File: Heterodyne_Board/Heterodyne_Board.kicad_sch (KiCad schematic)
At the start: 56 parts, among them J1 AVR-ISP-6, J2 Speaker, J3 SWITCH, J4 LED, J6 AudioJack2_Ground_Switch, J7 Barrel_Jack, SW1 SW_SPST, SW2 SW_SPST, U1 ATtiny85-20P, U2 TLV9054xD, U3 AP2112K-3.3, U4 LM386, U5 W25X40CLSN

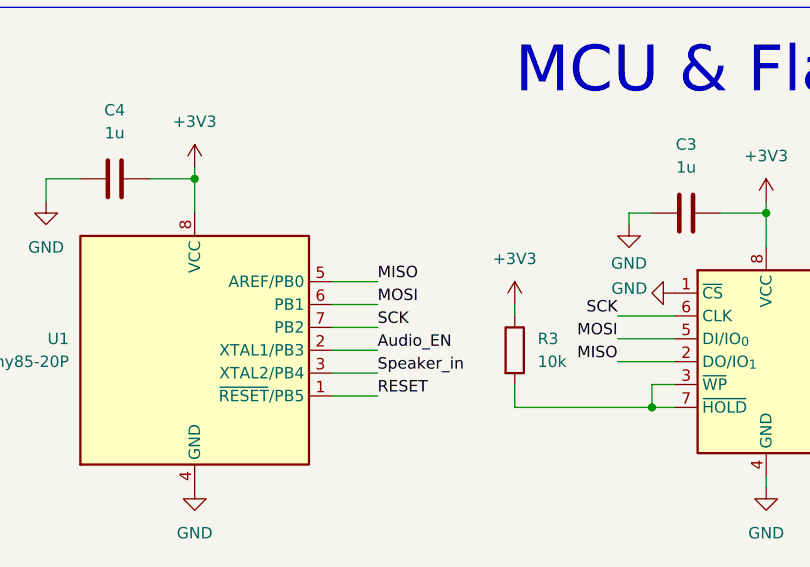
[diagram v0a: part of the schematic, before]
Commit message: Fixed MOSI/MISO line, lab entry for 3-1
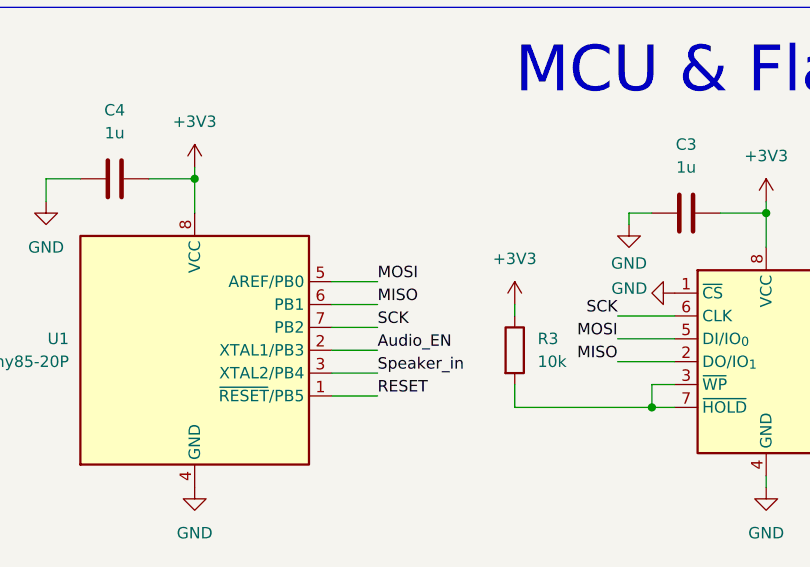
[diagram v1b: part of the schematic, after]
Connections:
- net MISO: now also U1.6 (PB1); no longer U1.5 (AREF/PB0)
- net MOSI: now also U1.5 (AREF/PB0); no longer U1.6 (PB1)
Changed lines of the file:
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@@
 		)
 	)
-	(label "MISO"
+	(label "MOSI"
 		(at 129.54 43.18 0)
 		(effects
@@
 		)
 	)
-	(label "MOSI"
+	(label "MISO"
 		(at 129.54 45.72 0)
 		(effects

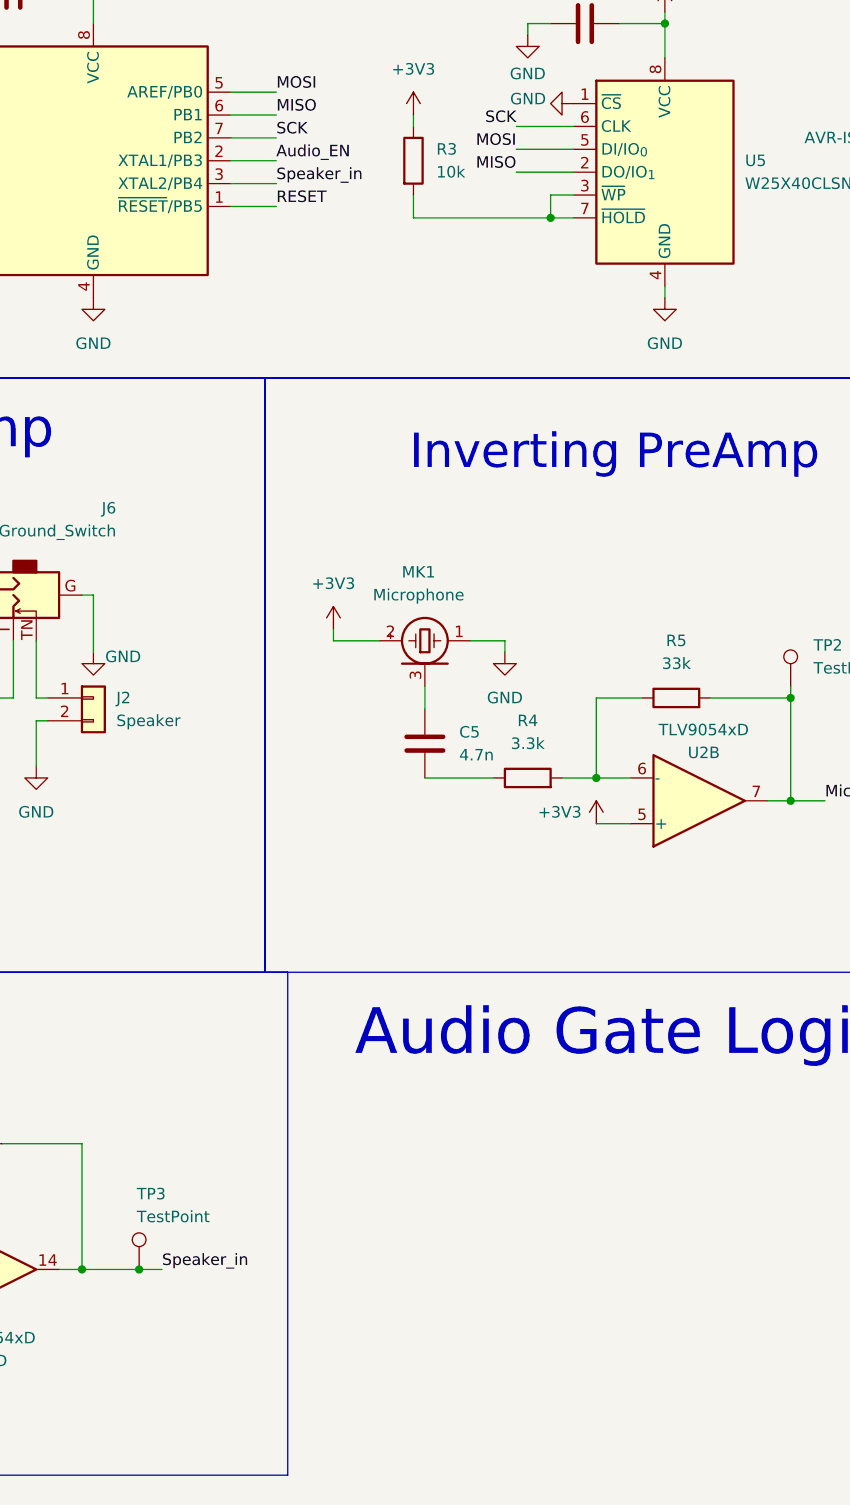
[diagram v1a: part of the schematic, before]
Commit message: added switch between mcu and mixer for audio output definition
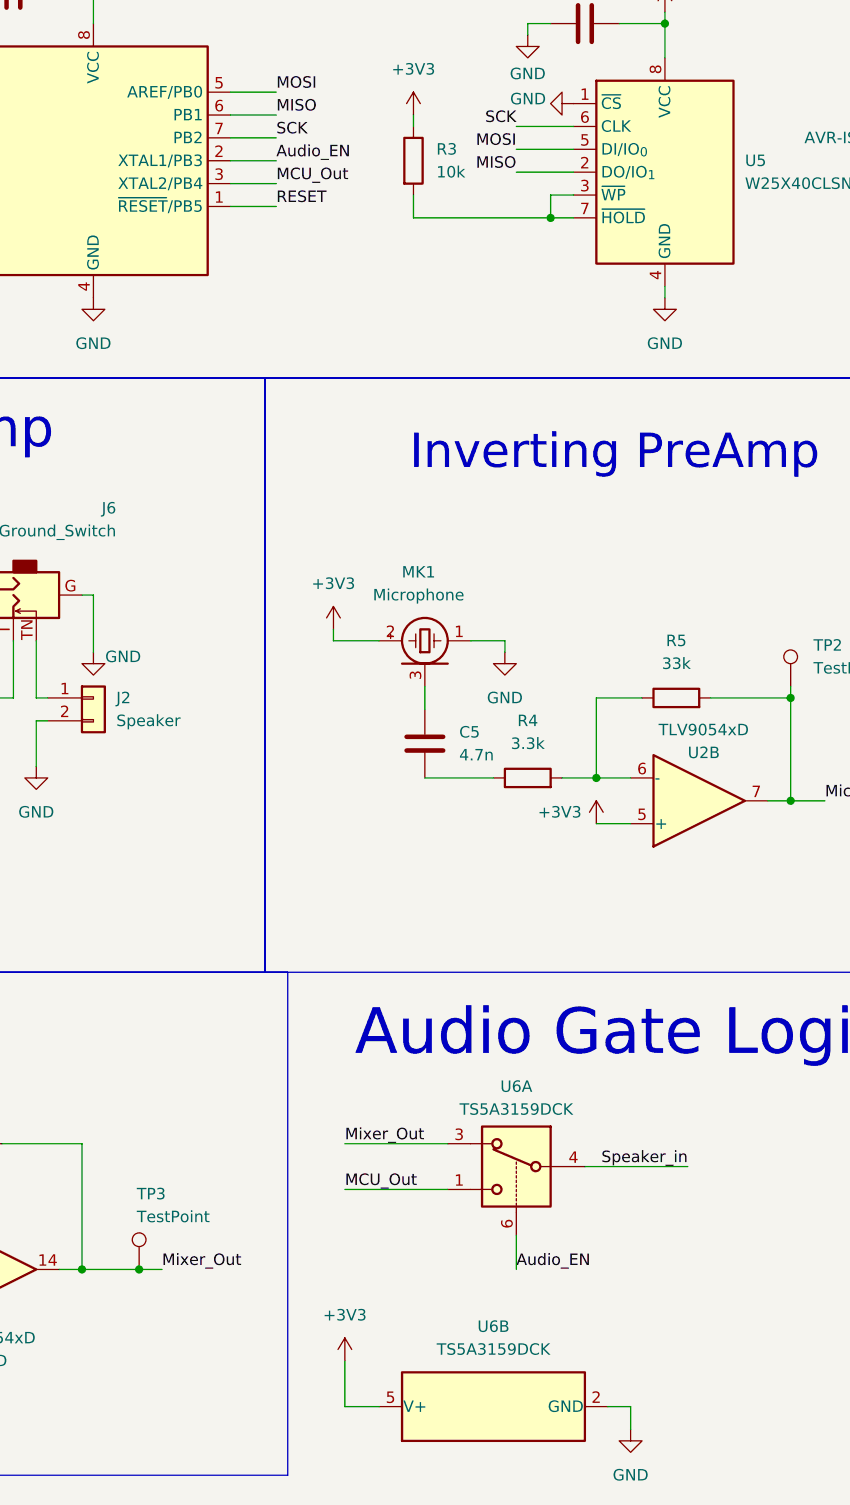
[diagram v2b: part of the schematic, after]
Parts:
- added U6: TS5A3159DCK, Package_TO_SOT_SMD:SOT-363_SC-70-6, symbol Analog_Switch:TS5A3159DCK
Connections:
- net +3V3: now also U6.5 (V+)
- net Audio_EN: now also U6.6
- net GND: now also U6.2 (GND)
- net Speaker_in: now also U6.4; no longer R16.2, TP3.1, U1.3 (XTAL2/PB4), U2.14
- new net MCU_Out: U1.3 (XTAL2/PB4), U6.1
- new net Mixer_Out: R16.2, TP3.1, U2.14, U6.3

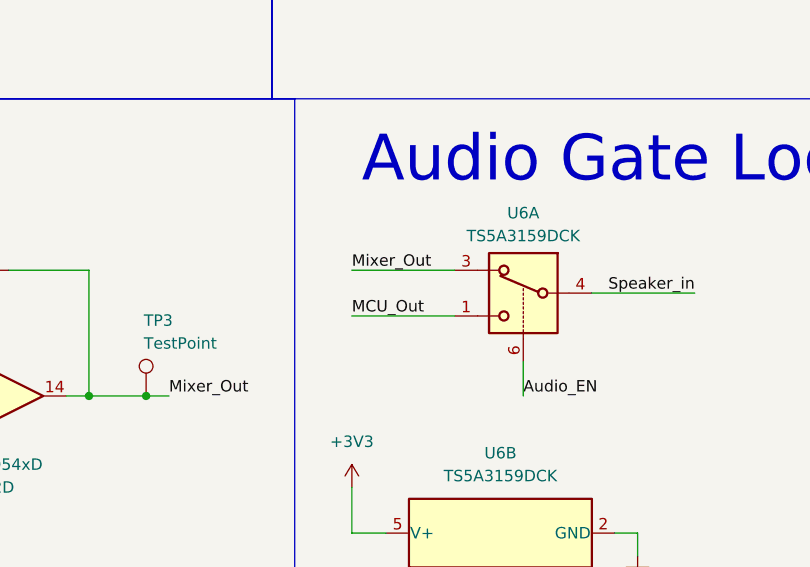
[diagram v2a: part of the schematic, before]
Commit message: added subboards under motherboard file, began firmware dev, flipped switch inputs
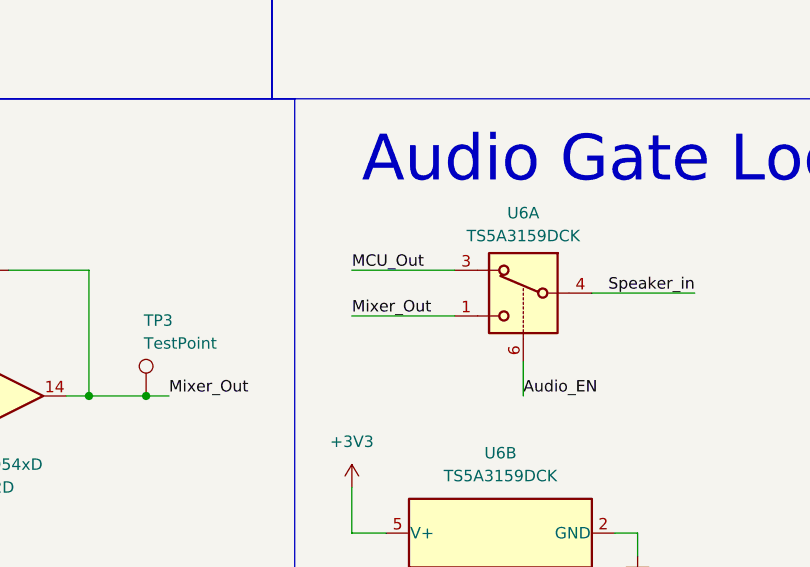
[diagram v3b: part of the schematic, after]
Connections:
- net MCU_Out: now also U6.3; no longer U6.1
- net Mixer_Out: now also U6.1; no longer U6.3
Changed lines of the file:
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@@
+		)
+	)
+	(label "Mixer_Out"
+		(at 137.16 165.1 0)
+		(effects
+			(font
+				(size 1.27 1.27)
+			)
+			(justify left bottom)
 		)
 	)
@@
 		)
 	)
-	(label "Mixer_Out"
-		(at 137.16 160.02 0)
-		(effects
-			(font
-				(size 1.27 1.27)
-			)
-			(justify left bottom)
-		)
-	)
 	(label "MOSI"
 		(at 156.21 49.53 180)
@@
 	)
 	(label "MCU_Out"
-		(at 137.16 165.1 0)
+		(at 137.16 160.02 0)
 		(effects
 			(font

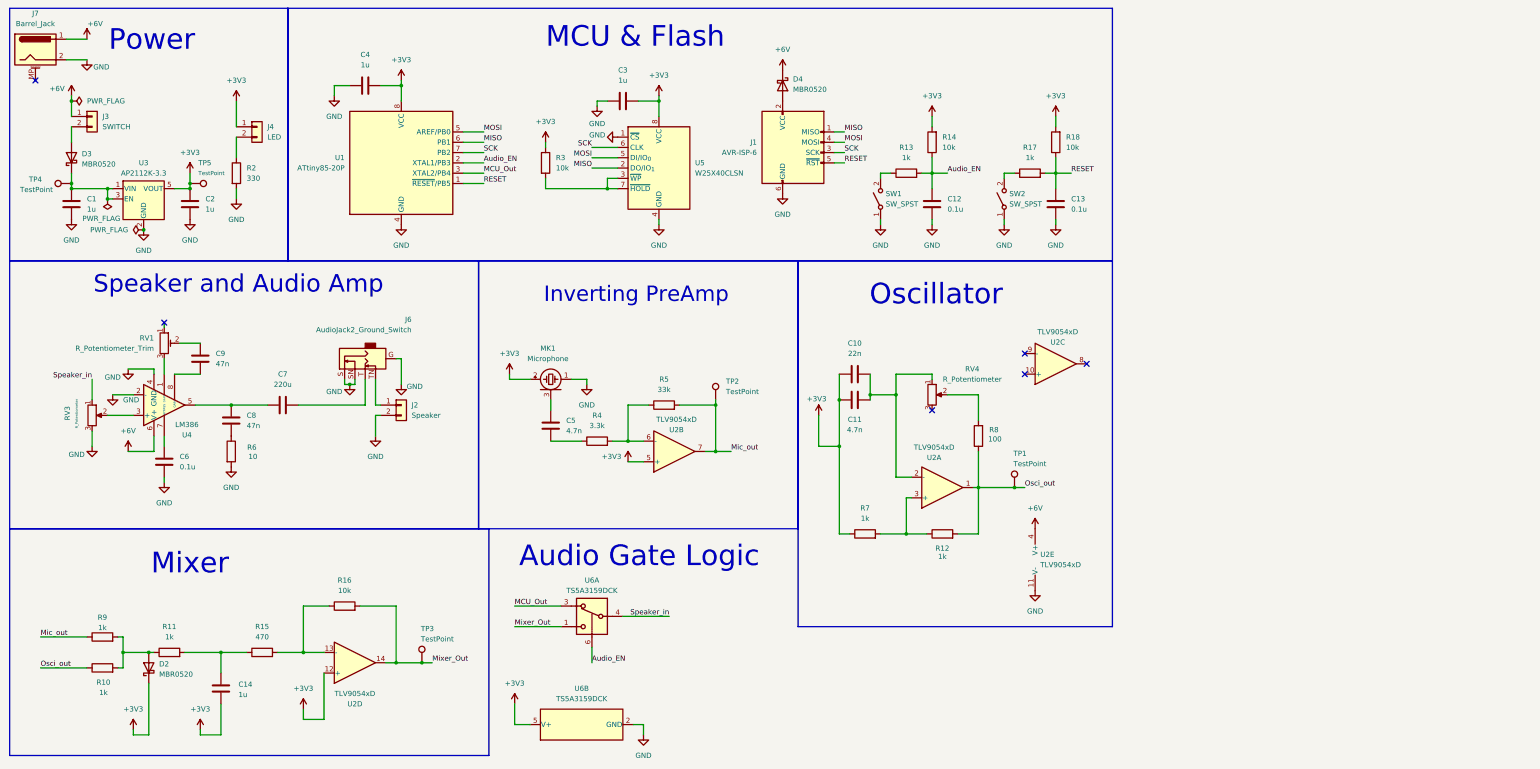
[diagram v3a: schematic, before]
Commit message: Board round 2 complete, GBRs sent
Also removed some of the automatic backups cuz they weren't necessary. Made discrete footprint for microphone
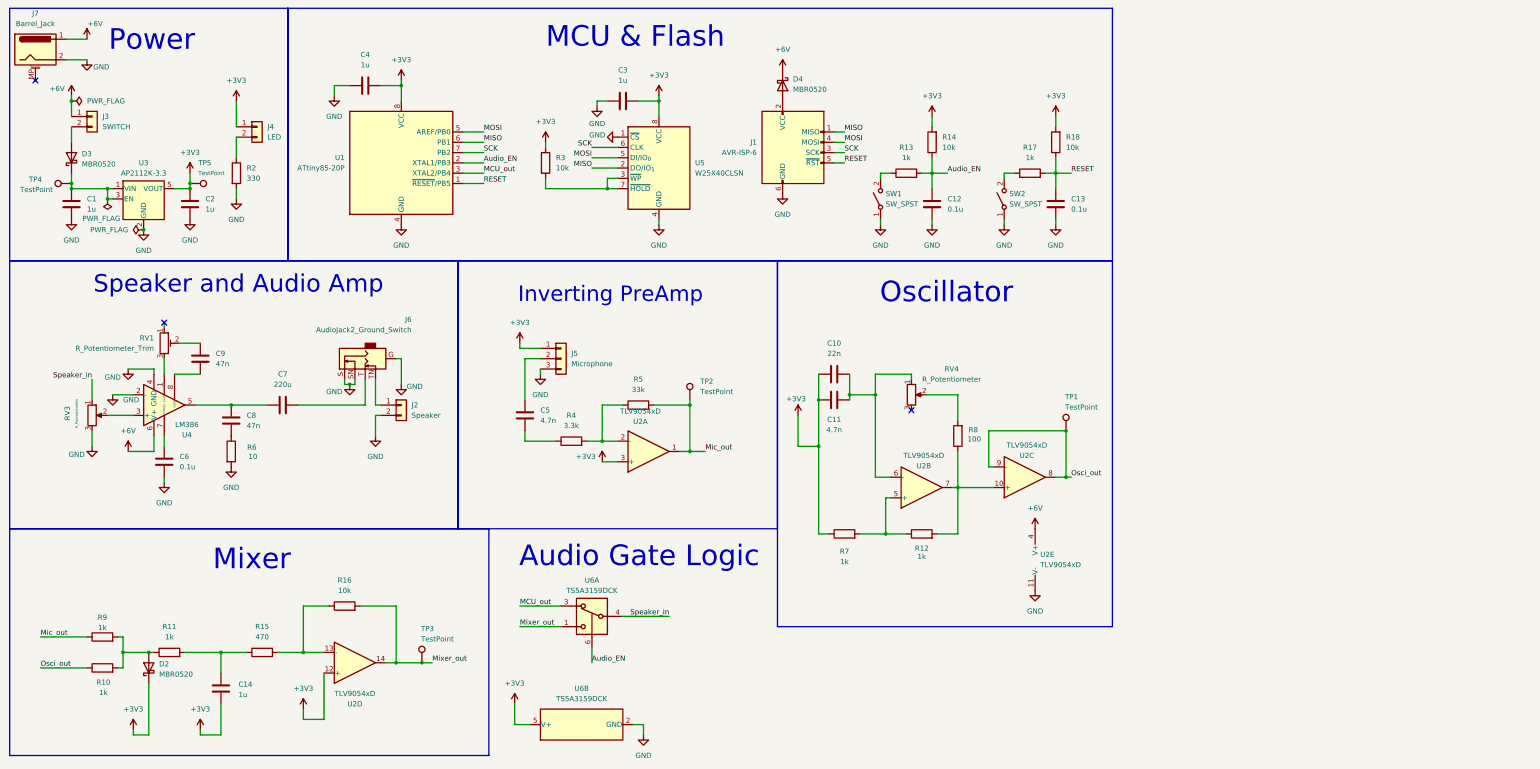
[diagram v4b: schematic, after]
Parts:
- removed MK1: Microphone, Sensor_Audio:Knowles_LGA-5_3.5x2.65mm, symbol Device:Microphone_Ultrasound
- added J5: Microphone, Connector_Molex:Molex_KK-254_AE-6410-03A_1x03_P2.54mm_Vertical, symbol Connector_Generic:Conn_01x03
- C7: footprint Capacitor_SMD:C_0805_2012Metric_Pad1.18x1.45mm_HandSolder -> Capacitor_THT:C_Radial_D6.3mm_H11.0mm_P2.50mm
- RV1: footprint Potentiometer_SMD:Potentiometer_Bourns_3269W_Vertical -> Potentiometer_SMD:Potentiometer_Bourns_TC33X_Vertical
- SW1, SW2: footprint Button_Switch_THT:SW_PUSH_6mm_H13mm -> Button_Switch_THT:SW_PUSH_6mm_H5mm
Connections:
- net +3V3: now also U2.3 (+), J5.1 (Pin_1); no longer U2.5 (+)
- net GND: now also J5.3 (Pin_3)
- net Mic_out: now also U2.1; no longer U2.7
- net Osci_out: now also U2.8, U2.9 (-); no longer R12.2, R8.1, U2.1
- net at C10.2, C11.2, RV4.1: now also U2.6 (-); no longer U2.2 (-)
- net at R12.1, R7.2: now also U2.5 (+); no longer U2.3 (+)
- net at C5.1: now also J5.2 (Pin_2)
- net at U2.10 (+): now also R12.2, R8.1, U2.7
- net at R4.2, R5.1: now also U2.2 (-); no longer U2.6 (-)
- net MCU_Out renamed MCU_out
- net Mixer_Out renamed Mixer_out
- no-connect marks 6 -> 3
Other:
- moved on the sheet: C10, C11, C5, R12, R4, R5, R7, R8, RV4, TP1, TP2

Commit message: Updated PCB
Mounting holes, second ISP header, wider board. Total dimensions about 70x70mm now.
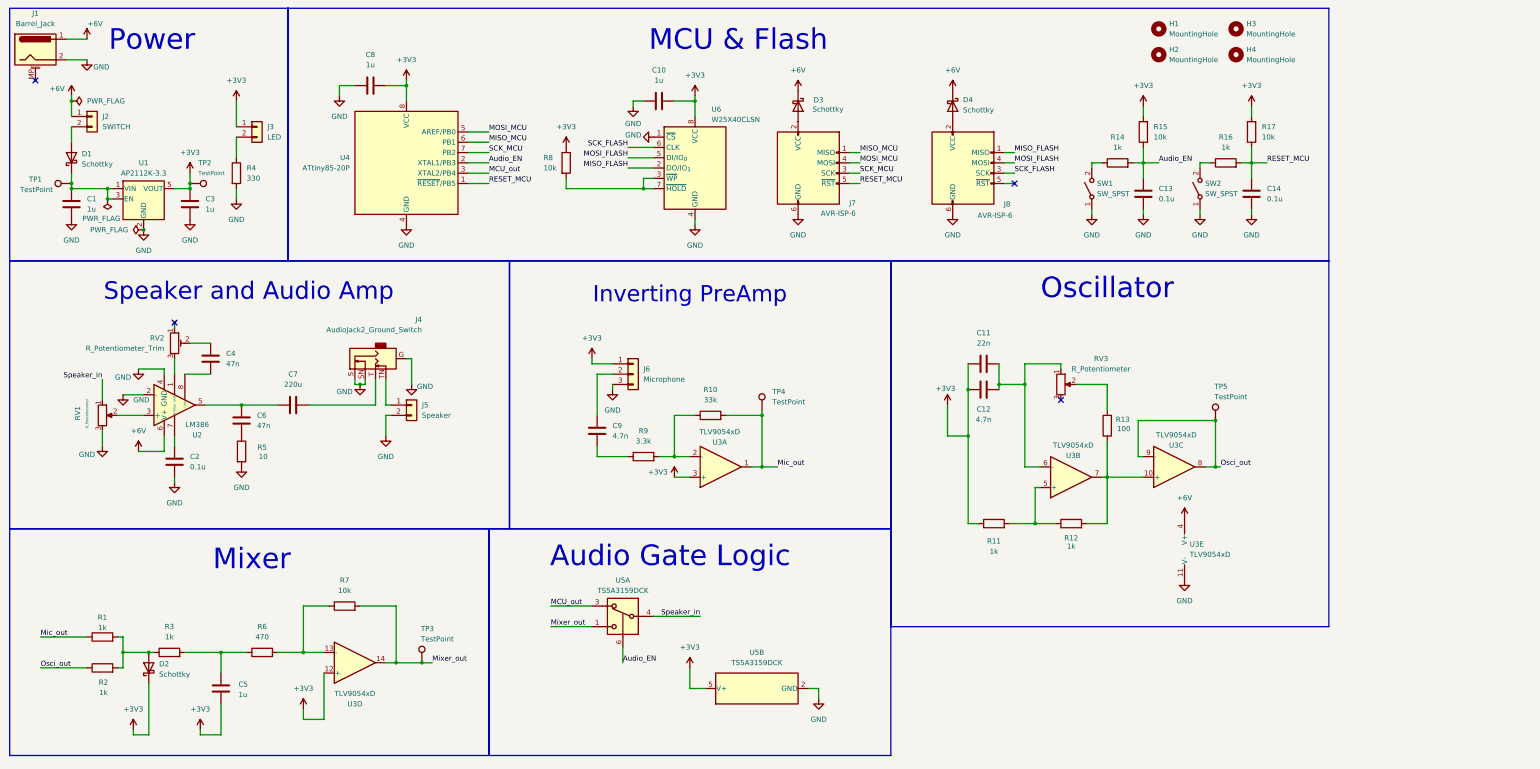
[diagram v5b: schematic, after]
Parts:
- added D4: Schottky, Diode_SMD:D_SOD-123, symbol Diode:MBR0520
- added H1, H2, H3, H4: MountingHole, MountingHole:MountingHole_3.2mm_M3, symbol Mechanical:MountingHole
- added J8: AVR-ISP-6, Connector_IDC:IDC-Header_2x03_P2.54mm_Vertical, symbol Connector:AVR-ISP-6
- D1: renamed from D3; value MBR0520 -> Schottky
- D2: value MBR0520 -> Schottky
- D3: renamed from D4; value MBR0520 -> Schottky
- renumbered C3 to C10, C10 to C11, C11 to C12, C12 to C13, C13 to C14, C6 to C2, C2 to C3, C9 to C4, C14 to C5, C8 to C6, C4 to C8, C5 to C9, J7 to J1, J3 to J2, J4 to J3, J6 to J4, J2 to J5, J5 to J6, J1 to J7, R9 to R1, R5 to R10, R7 to R11, R8 to R13, R13 to R14, R14 to R15, R17 to R16, R18 to R17, R10 to R2, R11 to R3, R2 to R4, R6 to R5, R15 to R6, R16 to R7, R3 to R8, R4 to R9, RV3 to RV1, RV1 to RV2, RV4 to RV3, TP4 to TP1, TP5 to TP2, TP2 to TP4, TP1 to TP5, U3 to U1, U4 to U2, U2 to U3, U1 to U4, U6 to U5, U5 to U6
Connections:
- net +6V: now also D4.1 (K)
- net GND: now also J8.6 (GND)
- net MISO renamed MISO_MCU
- net MISO_MCU: no longer U6.2 (DO/IO_{1})
- net MOSI renamed MOSI_MCU
- net MOSI_MCU: no longer U6.5 (DI/IO_{0})
- net RESET renamed RESET_MCU
- net SCK renamed SCK_MCU
- net SCK_MCU: no longer U6.6 (CLK)
- new net: D4.2 (A), J8.2 (VCC)
- new net MISO_FLASH: J8.1 (MISO), U6.2 (DO/IO_{1})
- new net MOSI_FLASH: J8.4 (MOSI), U6.5 (DI/IO_{0})
- new net SCK_FLASH: J8.3 (SCK), U6.6 (CLK)
- no-connect marks 3 -> 4
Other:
- moved on the sheet: C10, C11, C12, C13, C14, C2, C4, C6, C7, C8, C9, D3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

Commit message: Round 3 PCB upload
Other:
- moved on the sheet: D2, TP1, TP2, U5A, U5B

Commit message: updated schematic a lil
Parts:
- added C15: 0.1u, Capacitor_SMD:C_0805_2012Metric_Pad1.18x1.45mm_HandSolder, symbol Device:C
- added R18: 1k, Resistor_SMD:R_0805_2012Metric_Pad1.20x1.40mm_HandSolder, symbol Device:R
- added R19: 10k, Resistor_SMD:R_0805_2012Metric_Pad1.20x1.40mm_HandSolder, symbol Device:R
- added SW3: SW_SPST, Button_Switch_THT:SW_PUSH_6mm_H5mm, symbol Switch:SW_SPST
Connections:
- net MISO_MCU is gone; now on net MISO: J7.1 (MISO), U4.6 (PB1)
- net MOSI_MCU is gone; now on net MOSI: J7.4 (MOSI), U4.5 (AREF/PB0)
- net SCK_MCU is gone; now on net SCK: J7.3 (SCK), U4.7 (PB2)
- net +3V3: now also R19.2
- net GND: now also C15.1, SW3.1 (A); no longer U6.1 (~{CS})
- net Chip_Select: now reaches J8.5 (~{RST})
- net Chip_Select: now also U6.1 (~{CS}), C15.2, R18.2, R19.1
- net MISO_FLASH renamed MISO
- net MISO: now also U6.5 (DI/IO_{0}); no longer U6.2 (DO/IO_{1})
- net MOSI_FLASH renamed MOSI
- net MOSI: now also U6.2 (DO/IO_{1}); no longer U6.5 (DI/IO_{0})
- net RESET_MCU renamed RESET
- net SCK_FLASH renamed SCK
- new net: R18.1, SW3.2 (B)
- no-connect marks 4 -> 3
